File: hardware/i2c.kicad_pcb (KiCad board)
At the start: 2 copper layers, 11 parts, among them P1 USB_B, P2 CONN_01X11, U1 CP2112

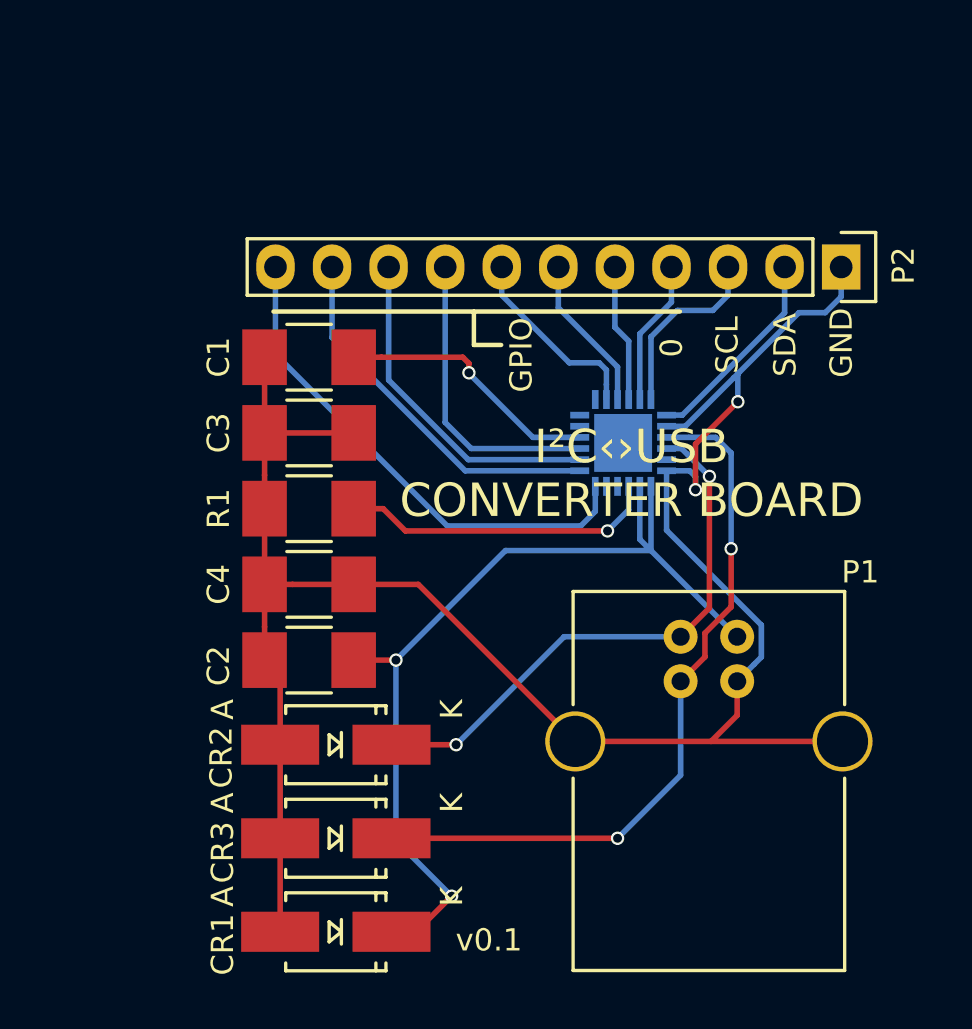
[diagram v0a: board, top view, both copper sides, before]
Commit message: Expose more pins on the board.
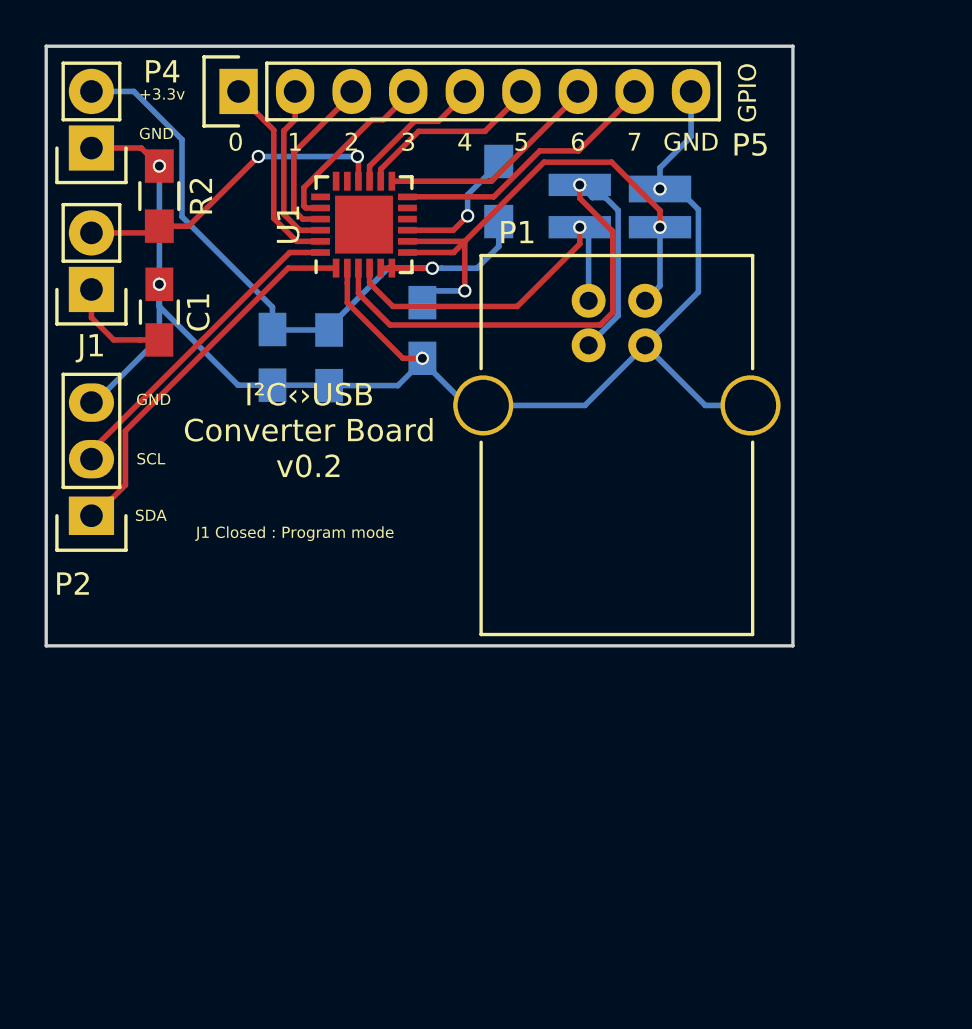
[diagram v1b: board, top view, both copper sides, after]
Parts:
- removed CR2, CR3: ESD, Diodes_SMD:SMA_Handsoldering
- added J1: CONN_01X02, Pin_Headers:Pin_Header_Straight_1x02, F.Cu at (147.8, 95.8)
- added P4: CONN_01X02, Pin_Headers:Pin_Header_Straight_1x02, F.Cu at (147.8, 89.4)
- added P5: CONN_01X09, Pin_Headers:Pin_Header_Straight_1x09, F.Cu at (154.4, 86.9)
- added R2: 10kΩ, Resistors_SMD:R_0805_HandSoldering, F.Cu at (150.9, 91.6)
- C1: footprint Capacitors_SMD:C_1210_HandSoldering -> Capacitors_SMD:C_0805_HandSoldering
- C2, C3, C4: footprint Capacitors_SMD:C_1210_HandSoldering -> Capacitors_SMD:C_0805_HandSoldering; moved to B.Cu
- CR1: value ESD -> SP0503BAHTG; footprint Diodes_SMD:SMA_Handsoldering -> TO_SOT_Packages_SMD:SOT-143_Handsoldering; moved to B.Cu
- P2: value CONN_01X11 -> CONN_01X03; footprint Pin_Headers:Pin_Header_Straight_1x11 -> Pin_Headers:Pin_Header_Straight_1x03
- R1: footprint Resistors_SMD:R_1210_HandSoldering -> Resistors_SMD:R_0805_HandSoldering; moved to B.Cu
- U1: moved to F.Cu
- moved P2 35.5 mm to (147.8, 105.9), turned to 180 degrees
- moved CR1 35.0 mm to (171.6, 92.0), turned to 270 degrees
- moved R1 16.6 mm to (166.1, 91.4), turned to 90 degrees
- moved C2 15.7 mm to (162.7, 97.6), turned to 270 degrees
- moved P1 15.6 mm to (172.7, 96.3)
- moved U1 15.2 mm to (160.1, 92.8), turned to 90 degrees
- moved C4 10.2 mm to (158.5, 98.8), turned to 270 degrees
- moved C1 7.02 mm to (150.9, 96.8), turned to 90 degrees
- moved C3 3.77 mm to (156.0, 98.8), turned to 270 degrees
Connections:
- C1 pad 1: GND -> /VPP
- C1 pad 2: Net-(C1-Pad2) -> GND
- C2 pad 1: Net-(C2-Pad1) -> /VCC
- C3 pad 1: GND -> /VDD
- C4 pad 1: GND -> /VDD
- CR1 pad 1: Net-(C2-Pad1) -> GND
- CR1 pad 2: GND -> /VCC
- P1 pad 1: Net-(C2-Pad1) -> /VCC
- P1 pad 2: Net-(CR2-Pad1) -> /D-
- P1 pad 3: Net-(CR3-Pad1) -> /D+
- P2 pad 1: GND -> /SDA
- P2 pad 2: Net-(P2-Pad2) -> /SCL
- P2 pad 3: Net-(P2-Pad3) -> GND
- R1 pad 1: GND -> /VDD
- U1 pad 1: Net-(P2-Pad2) -> /SDA
- U1 pad 12: Net-(P2-Pad11) -> /GPIO.7
- U1 pad 13: Net-(P2-Pad10) -> /GPIO.6
- U1 pad 14: Net-(P2-Pad9) -> /GPIO.5
- U1 pad 15: Net-(P2-Pad8) -> /GPIO.4
- U1 pad 16: Net-(C1-Pad2) -> /VPP
- U1 pad 20: Net-(P2-Pad7) -> /GPIO.3
- U1 pad 21: Net-(P2-Pad6) -> /GPIO.2
- U1 pad 22: Net-(P2-Pad5) -> /GPIO.1
- U1 pad 23: Net-(P2-Pad4) -> /GPIO.0
- U1 pad 24: Net-(P2-Pad3) -> /SCL
- U1 pad 3: Net-(CR3-Pad1) -> /D+
- U1 pad 4: Net-(CR2-Pad1) -> /D-
- U1 pad 5: GND -> /VDD
- U1 pad 6: GND -> /VDD
- U1 pad 7: Net-(C2-Pad1) -> /VCC
- U1 pad 8: Net-(C2-Pad1) -> /VCC
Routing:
- net Net-(C2-Pad1): track 41.8 -> 0.00 mm, vias 2 -> 0
- net Net-(CR3-Pad1): track 32.8 -> 0.00 mm, vias 2 -> 0
- net /VDD: track 0.00 -> 30.4 mm, vias 0 -> 1
- net /D+: track 0.00 -> 28.5 mm, vias 0 -> 1
- net GND: track 93.5 -> 68.2 mm, vias 2 -> 4
- net /VCC: track 0.00 -> 25.2 mm, vias 0 -> 2
- net Net-(CR2-Pad1): track 25.2 -> 0.00 mm, vias 2 -> 0
- net Net-(P2-Pad11): track 22.9 -> 0.00 mm
- net /VPP: track 0.00 -> 19.2 mm, vias 0 -> 2
- net /SDA: track 0.00 -> 17.0 mm
- net Net-(P2-Pad10): track 16.8 -> 0.00 mm
- net /D-: track 0.00 -> 15.9 mm, vias 0 -> 1
- net Net-(P2-Pad9): track 15.1 -> 0.00 mm
- net /SCL: track 0.00 -> 14.4 mm
- net Net-(P2-Pad8): track 13.5 -> 0.00 mm
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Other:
- board outline added: 33.5 x 26.9 mm
- net class Ground added: clearance 0.2, trace_width 0.5, via_dia 0.6, via_drill 0.4
- net class VCC added: clearance 0.2, trace_width 0.3, via_dia 0.6, via_drill 0.4
- board text added: "+3.3v"
- board text added: "1"
- board text added: "2"
- board text added: "3"
- board text added: "4"
- board text added: "5"
- board text added: "6"
- board text added: "7"
- board text added: "I²C‹›USB Converter Board v0.2"
- board text added: "J1 Closed : Program mode"
- board text removed: "I²C‹›USB CONVERTER BOARD"
- board text removed: "v0.1"

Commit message: Move U1 passives closer to the IC.
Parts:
- moved C3 4.79 mm to (160.6, 97.6)
- moved C4 1.23 mm to (158.5, 97.6)
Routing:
- net GND: track 68.2 -> 65.6 mm
- net /VDD: track 30.4 -> 29.3 mm
